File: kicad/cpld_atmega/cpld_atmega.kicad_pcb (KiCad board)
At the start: 2 copper layers, 106.7 x 58.4 mm, 33 parts, among them CON1 AVR-ISP-6, J1 PWR, J10 FB 4, J2 ADC, J3 Port B, J4 PORT D, J5 Port C, J6 FB 1, J7 FB 2, J8 JTAG, J9 FB 3, SW1 SW_Push, SW2 PWR, U1 LM1117-3.3, U2 ATMEGA168A-AU, U3 XC9572XL-VQFP44, Y1 12Mhz

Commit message: 1.version almost done
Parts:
- J1: footprint Connectors_Hirose:Hirose_DF63-2P-3.96DSA_02x3.96mm_Straight -> Connectors:JWT_Vertical_A3963-RM3.96mm-2
- moved C1 15.0 mm to (37.2, 66.4), turned to 90 degrees
- moved C8 10.8 mm to (28.4, 74.7), turned to 0 degrees
- moved CON1 9.64 mm to (31.2, 80.5)
- moved R3 9.07 mm to (58.2, 52.1), turned to 180 degrees
- moved J3 8.52 mm to (51.1, 89.2)
- moved J2 8.36 mm to (45.7, 52.8), turned to 270 degrees
- moved C5 5.31 mm to (40.3, 56.5), turned to 0 degrees
- moved R1 4.70 mm to (29.7, 72.1)
- moved U1 3.45 mm to (27.4, 57.7)
- moved SW2 3.30 mm to (35.2, 57.4)
- moved J5 2.44 mm to (41.8, 48.1)
- moved C6 2.44 mm to (27.1, 49.9)
- moved C9 1.81 mm to (26.2, 67.8), turned to 90 degrees
- moved Y1 0.54 mm to (56.5, 77.0)
- moved R6 0.51 mm to (73.5, 80.9)
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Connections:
- J8 pad 6: Net-(J8-Pad6) -> (no net)
- J8 pad 7: Net-(J8-Pad7) -> (no net)
- J8 pad 8: Net-(J8-Pad8) -> (no net)
- SW2 pad 1: (no net) -> Net-(SW2-Pad1)
- SW2 pad 6: (no net) -> Net-(SW2-Pad6)
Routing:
- net VCC: track 180.8 -> 352.4 mm, vias 3 -> 8
- net GND: track 15.1 -> 156.6 mm
- net +2V5: track 10.6 -> 30.6 mm, vias 0 -> 2
- net /SCK: track 94.9 -> 75.3 mm
- net Net-(J2-Pad3): track 0.00 -> 15.0 mm
- net Net-(R7-Pad1): track 17.7 -> 32.5 mm
- net /MISO: track 114.2 -> 99.8 mm, vias 0 -> 2
- net /RESET: track 84.2 -> 71.6 mm
- net Net-(J2-Pad2): track 0.00 -> 11.2 mm
- net Net-(R3-Pad2): track 4.79 -> 15.5 mm
- net /MOSI_: track 58.0 -> 66.3 mm
- net Net-(J3-Pad2): track 30.8 -> 22.9 mm
- net Net-(J3-Pad4): track 30.1 -> 22.5 mm
- net Net-(J3-Pad3): track 29.9 -> 22.7 mm
- net /TDI: track 44.1 -> 37.9 mm
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- added copper zone on F.Cu, net GND
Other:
- board size 106.7 x 58.4 mm -> 82.5 x 52.7 mm

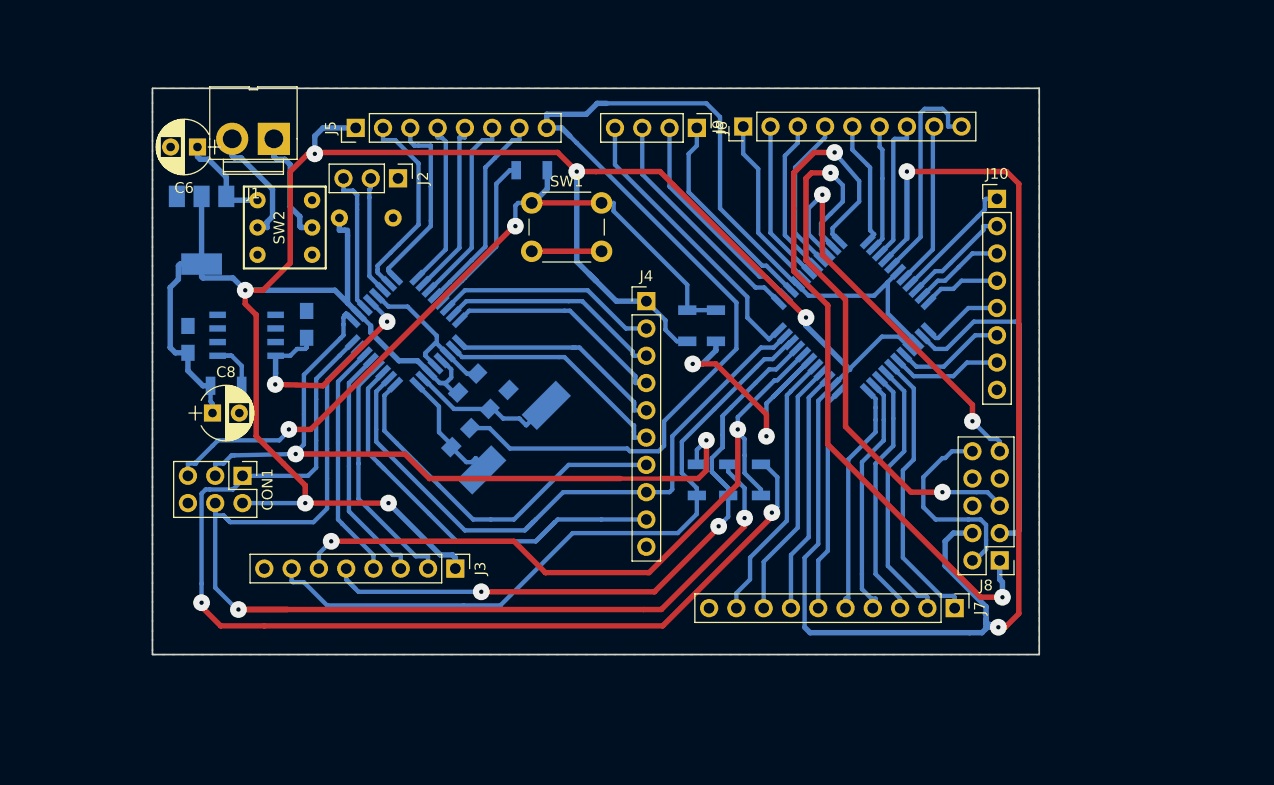
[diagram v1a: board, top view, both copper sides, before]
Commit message: label s are added
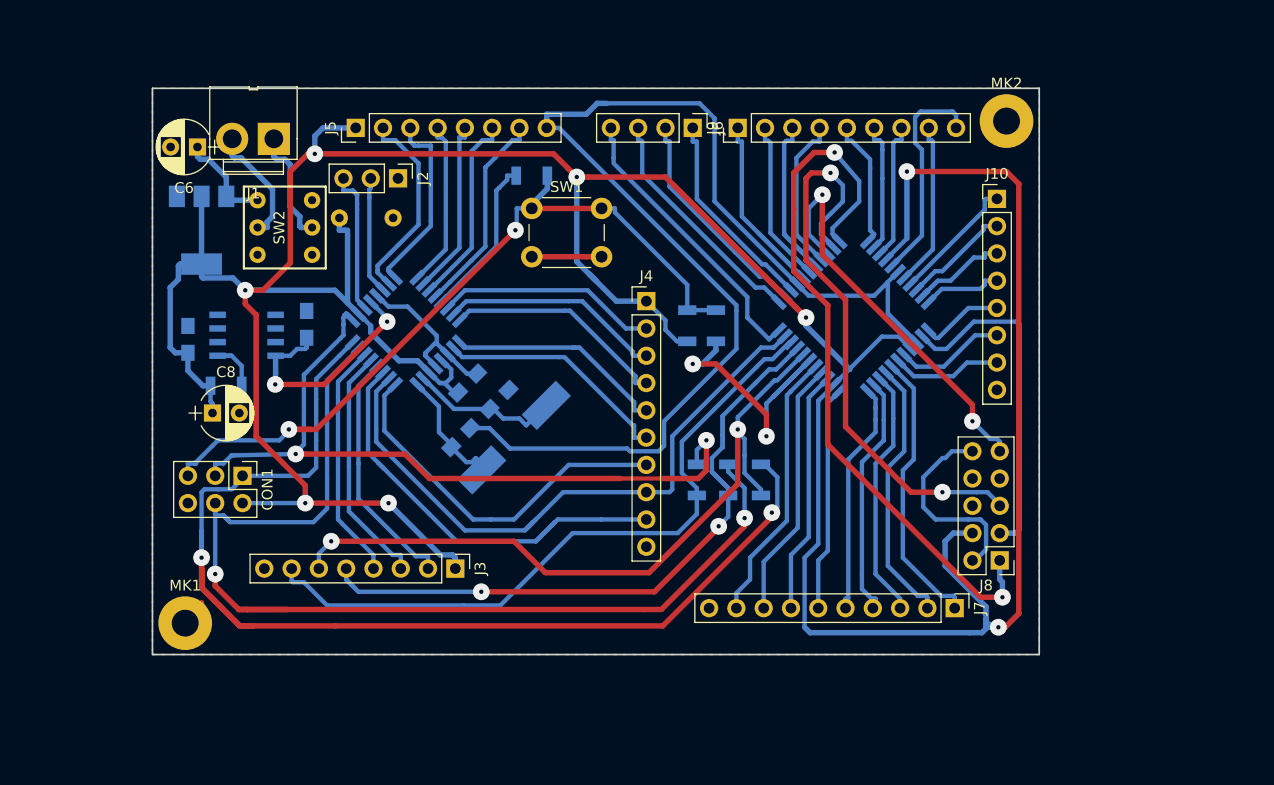
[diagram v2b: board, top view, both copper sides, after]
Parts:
- added MK1: MH, MountingHole:MountingHole_2.5mm_Pad, F.Cu at (25.9, 94.2)
- added MK2: MH, MountingHole:MountingHole_2.5mm_Pad, F.Cu at (102.4, 47.5)
- moved J9 0.52 mm to (77.3, 48.1)
- moved R3 0.51 mm to (58.2, 52.6)
- moved SW1 0.51 mm to (58.2, 55.6)
- moved J6 0.38 mm to (73.2, 48.1)
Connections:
- SW2 pad 1: Net-(SW2-Pad1) -> (no net)
- SW2 pad 6: Net-(SW2-Pad6) -> (no net)
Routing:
- net VCC: track 352.4 -> 369.6 mm
- net /MISO: track 99.8 -> 113.5 mm
- net +2V5: track 30.6 -> 22.1 mm
- net Net-(J9-Pad1): track 16.4 -> 22.6 mm
- net Net-(J9-Pad3): track 14.7 -> 18.8 mm
- net Net-(J10-Pad3): track 8.58 -> 10.7 mm
- net /RESET: track 71.6 -> 73.3 mm
- net /MOSI: track 101.7 -> 102.5 mm
- net Net-(J9-Pad7): track 13.7 -> 13.0 mm
- net Net-(J9-Pad4): track 15.2 -> 14.5 mm
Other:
- board text added: "GND"
- board text added: "NC"
- board text added: "P1"
- board text added: "P12"
- board text added: "P13"
- board text added: "P14"
- board text added: "P16"
- board text added: "P18"
- board text added: "P19"
- board text added: "P2"
- board text added: "P20"
- board text added: "P21"
- board text added: "P22"
- board text added: "P23"
- board text added: "P27"
- board text added: "P28"
- board text added: "P29"
- board text added: "P3"
- board text added: "P30"
- board text added: "P33"
- board text added: "P34"
- board text added: "P36"
- board text added: "P37"
- board text added: "P38"
- board text added: "P39 = RESET P40 = MISO P41 = MOSI P42 = SCK P43 = CCLK"
- board text added: "P43"
- board text added: "P44"
- board text added: "P5"
- board text added: "P6"
- board text added: "P7"
- board text added: "P8"
- board text added: "PB0"
- board text added: "PB1"
- board text added: "PB2"
- board text added: "PB3/MOSI"
- board text added: "PB4/MISO"
- board text added: "PB5/SCK"
- board text added: "PC0"
- board text added: "PC1"
- board text added: "PC2"
- board text added: "PC3"
- board text added: "PC4"
- board text added: "PC5"
- board text added: "PC6"
- board text added: "PD1"
- board text added: "PD2"
- board text added: "PD3"
- board text added: "PD4"
- board text added: "PD5"
- board text added: "PD6"
- board text added: "PD7"
- board text added: "PWR"
- board text added: "RESET"
- board text added: "TCK"
- board text added: "TDI"
- board text added: "TDO"
- board text added: "TMS"
- board text added: "VCC"

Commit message: version 0.1
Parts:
- removed C5: 100n, Capacitors_THT:C_Disc_D4.3mm_W1.9mm_P5.00mm
- removed J8: JTAG, Pin_Headers:Pin_Header_Straight_2x05_Pitch2.54mm
- added C3: 100n, Capacitor_SMD:C_0805_2012Metric_Pad1.15x1.40mm_HandSolder, F.Cu at (61.6, 71.6)
- added G***: LOGO, custom_logo:pimium_paprika_7mm, F.Cu at (78.5, 61.8)
- added J11: Conn_01x11, Connector_PinSocket_2.54mm:PinSocket_1x11_P2.54mm_Vertical, F.Cu at (74.3, 56.1)
- added J12: JTAG, Connector_PinSocket_2.54mm:PinSocket_1x07_P2.54mm_Vertical, F.Cu at (95.6, 94.7)
- added R8: 470, Resistor_SMD:R_0603_1608Metric_Pad1.05x0.95mm_HandSolder, F.Cu at (74.3, 94.4)
- C1, C2, C7, U1, U2, Y1: moved to F.Cu
- C4, C9: footprint Capacitors_SMD:C_0805_HandSoldering -> Capacitor_SMD:C_0805_2012Metric_Pad1.15x1.40mm_HandSolder; moved to F.Cu
- D1: value TL431D -> LED; footprint Housings_SOIC:SOIC-8_3.9x4.9mm_Pitch1.27mm -> LED_SMD:LED_1206_3216Metric_Pad1.42x1.75mm_HandSolder; moved to F.Cu
- J1: footprint Connectors:JWT_Vertical_A3963-RM3.96mm-2 -> TerminalBlock_RND:TerminalBlock_RND_205-00001_1x02_P5.00mm_Horizontal
- J10: value FB 4 -> Conn_01x11; footprint Pin_Headers:Pin_Header_Straight_1x08_Pitch2.54mm -> Connector_PinSocket_2.54mm:PinSocket_1x11_P2.54mm_Vertical
- J2: value ADC -> Conn_01x08_Male; footprint Pin_Headers:Pin_Header_Straight_1x03_Pitch2.54mm -> Connector_PinSocket_2.54mm:PinSocket_1x08_P2.54mm_Vertical
- J3: value Port B -> Conn_01x08_Male; footprint Pin_Headers:Pin_Header_Straight_1x08_Pitch2.54mm -> Connector_PinSocket_2.54mm:PinSocket_1x08_P2.54mm_Vertical
- J4: value PORT D -> Conn_01x08_Male; footprint Pin_Headers:Pin_Header_Straight_1x10_Pitch2.54mm -> Connector_PinSocket_2.54mm:PinSocket_1x08_P2.54mm_Vertical
- J5: value Port C -> Conn_01x08_Male; footprint Pin_Headers:Pin_Header_Straight_1x08_Pitch2.54mm -> Connector_PinSocket_2.54mm:PinSocket_1x08_P2.54mm_Vertical
- J6: value FB 1 -> Conn_01x11; footprint Pin_Headers:Pin_Header_Straight_1x04_Pitch2.54mm -> Connector_PinSocket_2.54mm:PinSocket_1x11_P2.54mm_Vertical
- J7: value FB 2 -> CLOCK; footprint Pin_Headers:Pin_Header_Straight_1x10_Pitch2.54mm -> Connector_PinSocket_2.54mm:PinSocket_1x03_P2.54mm_Vertical
- J9: value FB 3 -> Conn_01x11; footprint Pin_Headers:Pin_Header_Straight_1x09_Pitch2.54mm -> Connector_PinSocket_2.54mm:PinSocket_1x11_P2.54mm_Vertical
- R1: value 1k -> 0; footprint Resistors_SMD:R_1206 -> Resistor_SMD:R_0805_2012Metric_Pad1.15x1.40mm_HandSolder; moved to F.Cu
- R2: value 4k7 -> 10K; footprint Resistors_SMD:R_1206 -> Resistor_SMD:R_0603_1608Metric_Pad1.05x0.95mm_HandSolder; moved to F.Cu
- R3: value 4k7 -> 1k; footprint Resistors_SMD:R_1206 -> Resistor_SMD:R_0603_1608Metric_Pad1.05x0.95mm_HandSolder; moved to F.Cu
- R4, R5, R6: footprint Resistors_SMD:R_1206 -> Resistor_SMD:R_0603_1608Metric_Pad1.05x0.95mm_HandSolder; moved to F.Cu
- R7: value 4k7 -> 1K; footprint Resistors_SMD:R_1206 -> Resistor_SMD:R_0603_1608Metric_Pad1.05x0.95mm_HandSolder; moved to F.Cu
- U3: footprint Housings_QFP:LQFP-44_10x10mm_Pitch0.8mm -> Package_QFP:LQFP-44_10x10mm_P0.8mm; moved to F.Cu
- moved C9 63.5 mm to (89.4, 62.0), turned to 0 degrees
- moved D1 51.1 mm to (76.8, 91.3), turned to 180 degrees
- moved J6 47.6 mm to (98.7, 88.3)
- moved MK2 46.9 mm to (102.6, 94.4)
- moved J2 42.0 mm to (39.2, 94.4), turned to 90 degrees
- moved R3 39.4 mm to (65.5, 91.3), turned to 0 degrees
- moved C8 38.5 mm to (62.9, 57.4)
- moved J9 36.6 mm to (70.4, 84.1), turned to 180 degrees
- moved J7 34.8 mm to (62.7, 94.2), turned to 90 degrees
- moved R1 32.0 mm to (61.6, 69.3), turned to 180 degrees
- moved J4 30.3 mm to (38.9, 68.8)
- moved R7 28.0 mm to (72.4, 94.4), turned to 270 degrees
- moved J5 26.1 mm to (62.0, 64.6), turned to 270 degrees
- moved R2 22.3 mm to (50.4, 68.8)
- moved C6 15.5 mm to (33.7, 63.9)
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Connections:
- C1 pad 1: +2V5 -> VCC
- C2 pad 1: /XTAL1 -> /P8
- C7 pad 1: /XTAL2 -> /P7
- CON1 pad 3: /SCK -> /P17
- D1 pad 1: Net-(D1-Pad1) -> GND
- D1 pad 2: GND -> Net-(D1-Pad2)
- J10 pad 6: Net-(J10-Pad6) -> GND
- J10 pad 8: GND -> VCC
- J2 pad 1: GND -> /P9
- J2 pad 2: Net-(J2-Pad2) -> /P10
- J2 pad 3: Net-(J2-Pad3) -> /P11
- J3 pad 1: VCC -> /P17
- J3 pad 2: Net-(J3-Pad2) -> VCC
- J3 pad 3: Net-(J3-Pad3) -> /P19
- J3 pad 4: Net-(J3-Pad4) -> /P20
- J3 pad 5: /MOSI_ -> GND
- J3 pad 6: /MISO_ -> /P22
- J3 pad 7: /SCK_ -> /P23
- J3 pad 8: GND -> /P24
- J4 pad 1: VCC -> /P1
- J4 pad 2: Net-(J4-Pad2) -> /P2
- J4 pad 3: Net-(J4-Pad3) -> GND
- J4 pad 4: Net-(J4-Pad4) -> VCC
- J4 pad 5: Net-(J4-Pad5) -> GND
- J4 pad 6: Net-(J4-Pad6) -> VCC
- J4 pad 7: Net-(J4-Pad7) -> /P7
- J4 pad 8: /CCLK -> /P8
- J5 pad 1: VCC -> /P25
- J5 pad 2: /PC0 -> /P26
- J5 pad 3: /PC1 -> /P27
- J5 pad 4: /PC2 -> /P28
- J5 pad 5: /PC3 -> /RESET
- J5 pad 6: /PC4 -> /P30
- J5 pad 7: /PC5 -> /P31
- J5 pad 8: GND -> /P32
- J6 pad 1: Net-(J6-Pad1) -> /TCK
- J6 pad 2: Net-(J6-Pad2) -> /TMS
- J6 pad 3: Net-(J6-Pad3) -> /TDI
- J7 pad 1: Net-(J7-Pad1) -> /P10
- J7 pad 3: Net-(J7-Pad3) -> /CCLK
- J9 pad 3: Net-(J9-Pad3) -> /P17
- J9 pad 4: Net-(J9-Pad4) -> /MOSI
- J9 pad 5: Net-(J9-Pad5) -> /MISO
- R1 pad 2: Net-(D1-Pad1) -> /P20
- R3 pad 1: /RESET -> Net-(J7-Pad2)
- R3 pad 2: Net-(R3-Pad2) -> Net-(J9-Pad2)
- R4 pad 1: /MOSI_ -> Net-(R4-Pad1)
- R5 pad 1: /MISO_ -> Net-(R5-Pad1)
- R6 pad 1: /SCK_ -> Net-(R6-Pad1)
- R6 pad 2: /SCK -> /P17
- R7 pad 1: Net-(R7-Pad1) -> Net-(J6-Pad10)
- U2 pad 1: Net-(J4-Pad5) -> /P1
- U2 pad 10: /CCLK -> /P10
- U2 pad 11: Net-(J4-Pad9) -> /P11
- U2 pad 12: Net-(J3-Pad2) -> /CCLK
- U2 pad 13: Net-(J3-Pad3) -> /P13
- U2 pad 14: Net-(J3-Pad4) -> /P14
- U2 pad 17: /SCK -> /P17
- U2 pad 19: Net-(J2-Pad3) -> /P19
- U2 pad 2: Net-(J4-Pad6) -> /P2
- U2 pad 20: +2V5 -> /P20
- U2 pad 22: Net-(J2-Pad2) -> /P22
- U2 pad 23: /PC0 -> /P23
- U2 pad 24: /PC1 -> /P24
- U2 pad 25: /PC2 -> /P25
- U2 pad 26: /PC3 -> /P26
- U2 pad 27: /PC4 -> /P27
- U2 pad 28: /PC5 -> /P28
- U2 pad 29: Net-(R3-Pad2) -> /RESET
- U2 pad 30: Net-(J4-Pad2) -> /P30
- U2 pad 31: Net-(J4-Pad3) -> /P31
- U2 pad 32: Net-(J4-Pad4) -> /P32
- U2 pad 7: /XTAL2 -> /P7
- U2 pad 8: /XTAL1 -> /P8
- U2 pad 9: Net-(J4-Pad7) -> /P9
- U3 pad 1: Net-(J6-Pad3) -> Net-(J6-Pad11)
- U3 pad 12: Net-(J9-Pad5) -> Net-(J10-Pad11)
- U3 pad 13: Net-(J9-Pad6) -> Net-(J10-Pad10)
- U3 pad 14: Net-(J9-Pad7) -> Net-(J10-Pad9)
- U3 pad 16: Net-(J9-Pad9) -> Net-(J10-Pad7)
- U3 pad 18: Net-(J9-Pad8) -> Net-(J10-Pad5)
- U3 pad 19: Net-(J10-Pad1) -> Net-(J10-Pad4)
- U3 pad 2: Net-(J6-Pad2) -> Net-(J6-Pad10)
- U3 pad 20: Net-(J10-Pad2) -> Net-(J10-Pad3)
- U3 pad 21: Net-(J10-Pad3) -> Net-(J10-Pad2)
- U3 pad 22: Net-(J10-Pad4) -> Net-(J10-Pad1)
- U3 pad 23: Net-(J10-Pad5) -> Net-(J11-Pad11)
- U3 pad 27: Net-(J10-Pad6) -> Net-(J11-Pad7)
- U3 pad 28: Net-(J10-Pad7) -> Net-(J11-Pad6)
- U3 pad 29: Net-(J7-Pad1) -> Net-(J11-Pad5)
- U3 pad 3: Net-(J6-Pad1) -> Net-(J6-Pad9)
- U3 pad 30: Net-(J7-Pad2) -> Net-(J11-Pad4)
- U3 pad 31: Net-(J7-Pad3) -> Net-(J11-Pad3)
- U3 pad 32: Net-(J7-Pad4) -> Net-(J11-Pad2)
- U3 pad 33: Net-(J7-Pad5) -> Net-(J11-Pad1)
- U3 pad 34: Net-(J7-Pad6) -> Net-(J9-Pad11)
- U3 pad 36: Net-(J7-Pad7) -> Net-(J9-Pad9)
- U3 pad 37: Net-(J7-Pad8) -> Net-(J9-Pad8)
- U3 pad 38: Net-(J7-Pad9) -> Net-(J9-Pad7)
- U3 pad 39: Net-(R7-Pad1) -> Net-(J9-Pad6)
- U3 pad 40: /MISO_ -> Net-(R5-Pad1)
- U3 pad 41: /MOSI_ -> Net-(R4-Pad1)
- U3 pad 42: /SCK_ -> Net-(R6-Pad1)
- U3 pad 43: /CCLK -> Net-(J9-Pad2)
- U3 pad 44: Net-(J6-Pad4) -> Net-(J9-Pad1)
- U3 pad 5: Net-(J9-Pad1) -> Net-(J6-Pad7)
- U3 pad 6: Net-(J9-Pad2) -> Net-(J6-Pad6)
- U3 pad 7: Net-(J9-Pad3) -> Net-(J6-Pad5)
- U3 pad 8: Net-(J9-Pad4) -> Net-(J6-Pad4)
- Y1 pad 1: /XTAL1 -> /P8
- Y1 pad 2: /XTAL2 -> /P7
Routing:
- net VCC: track 369.6 -> 219.9 mm, vias 8 -> 0
- net GND: track 156.1 -> 254.8 mm
- net /P17: track 0.00 -> 78.5 mm
- net /SCK: track 75.3 -> 0.00 mm, vias 2 -> 0
- net /MISO_: track 67.3 -> 0.00 mm, vias 2 -> 0
- net /MOSI_: track 66.3 -> 0.00 mm, vias 2 -> 0
- net /SCK_: track 64.7 -> 0.00 mm
- net /TCK: track 73.6 -> 21.1 mm, vias 2 -> 0
- net Net-(J4-Pad9): track 41.6 -> 0.00 mm
- net /MISO: track 113.5 -> 75.2 mm, vias 2 -> 0
- net /P10: track 0.00 -> 37.4 mm
- net /RESET: track 73.3 -> 109.2 mm, vias 2 -> 0
- net Net-(J4-Pad7): track 34.6 -> 0.00 mm
- net /P7: track 0.00 -> 34.2 mm, vias 0 -> 1
- net /TMS: track 55.7 -> 21.9 mm, vias 2 -> 0
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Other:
- board size 82.5 x 52.7 mm -> 77.2 x 44.8 mm
- net class Default: clearance 0.2 -> 0.20066; trace_width 0.25 -> 0.254
- net class Signal: clearance 0.2 -> 0.20828
- rule trace_clearance: 0.2 -> 0.20066
- board text added: "CPLD_ATMEGA168 V.0.1"
- board text added: "PIN1"
- board text added: "VCC GND NC TDI TMS TDO TCK"
- board text removed: "GND"
- board text removed: "NC"
- board text removed: "P1"
- board text removed: "P12"
- board text removed: "P13"
- board text removed: "P14"
- board text removed: "P16"
- board text removed: "P18"
- board text removed: "P19"
- board text removed: "P2"
- board text removed: "P20"
- board text removed: "P21"
- board text removed: "P22"
- board text removed: "P23"
- board text removed: "P27"
- board text removed: "P28"
- board text removed: "P29"
- board text removed: "P3"
- board text removed: "P30"
- board text removed: "P33"
- board text removed: "P34"
- board text removed: "P36"
- board text removed: "P37"
- board text removed: "P38"
- board text removed: "P39 = RESET P40 = MISO P41 = MOSI P42 = SCK P43 = CCLK"
- board text removed: "P43"
- board text removed: "P44"
- board text removed: "P5"
- board text removed: "P6"
- board text removed: "P7"
- board text removed: "P8"
- board text removed: "PB0"
- board text removed: "PB1"
- board text removed: "PB2"
- board text removed: "PB3/MOSI"
- board text removed: "PB4/MISO"
- board text removed: "PB5/SCK"
- board text removed: "PC0"
- board text removed: "PC1"
- board text removed: "PC2"
- board text removed: "PC3"
- board text removed: "PC4"
- board text removed: "PC5"
- board text removed: "PC6"
- board text removed: "PD1"
- board text removed: "PD2"
- board text removed: "PD3"
- board text removed: "PD4"
- board text removed: "PD5"
- board text removed: "PD6"
- board text removed: "PD7"
- board text removed: "PWR"
- board text removed: "RESET"
- board text removed: "TCK"
- board text removed: "TDI"
- board text removed: "TDO"
- board text removed: "TMS"
- board text removed: "VCC"
